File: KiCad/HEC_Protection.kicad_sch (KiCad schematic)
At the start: 19 parts, among them U10 74LS32, U11 74LS00, U11 74LS32, U12 74LS04, U17 74LS74, U18 74LS138, U18 74LS74, U19 74LS30, U22 74LS02, U23 74LS74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

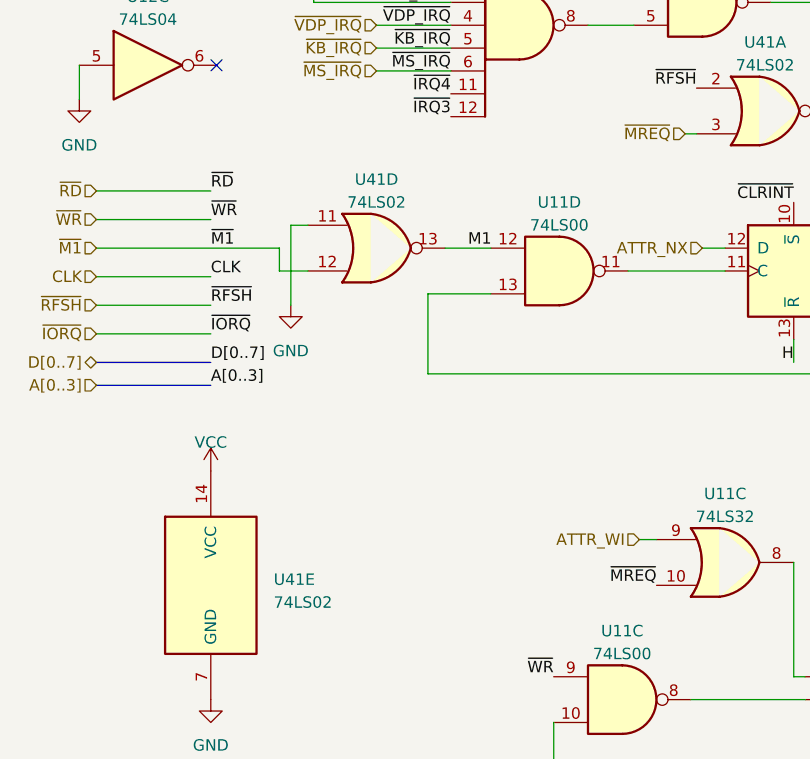
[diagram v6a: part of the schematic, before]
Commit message: Finish routing data bus
finished routing arguably the hardest part of the board: the data bus. The routing is mostly complete. However, the rest of traces are very hard to route. One more day of work is expected.
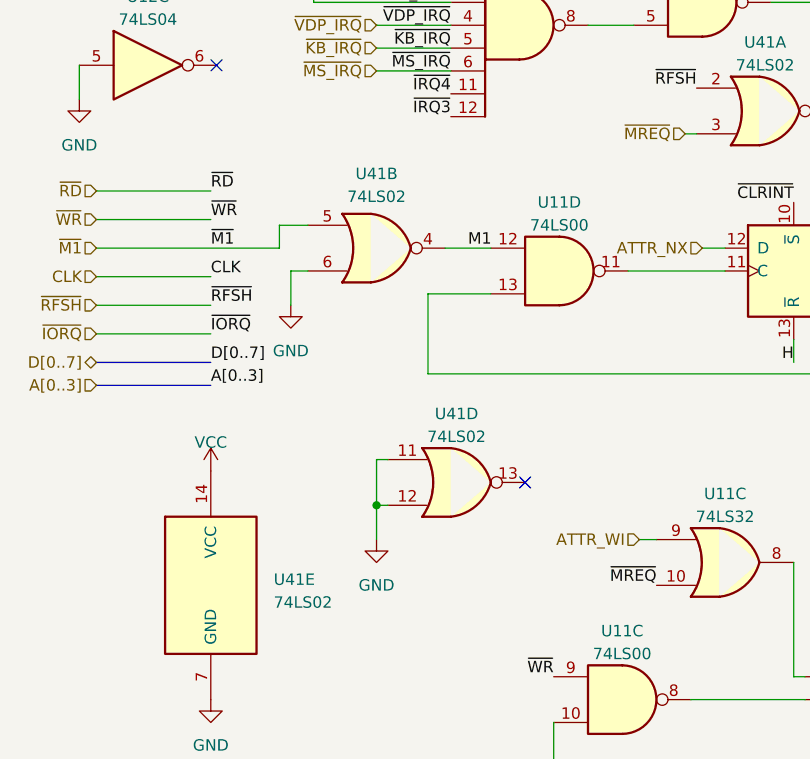
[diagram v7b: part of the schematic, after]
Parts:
- added unit 2 of U41
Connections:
- net GND: now also U41.12, U41.6
- net M1: now also U41.4; no longer U41.13
- net ~{M1}: now also U41.5; no longer U41.12
- no-connect marks 15 -> 16
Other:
- moved on the sheet: U41D
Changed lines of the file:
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@@
   (junction (at 234.315 45.085) (diameter 0) (color 0 0 0 0)
+  )
+  (junction (at 53.34 120.015) (diameter 0) (color 0 0 0 0)
   )
   (junction (at 121.285 139.065) (diameter 0) (color 0 0 0 0)
@@
   (no_connect (at 40.005 36.195))
   (no_connect (at 262.89 90.17))
+  (no_connect (at 69.85 117.475))
   (no_connect (at 165.735 96.52))
   (no_connect (at 116.205 144.145))
@@
     (stroke (width 0) (type default))
   )
+  (wire (pts (xy 53.34 120.015) (xy 54.61 120.015))
+    (stroke (width 0) (type default))
+  )
   (bus (pts (xy 244.475 128.905) (xy 244.475 131.445))
     (stroke (width 0) (type default))
@@
     (stroke (width 0) (type default))
   )
+  (wire (pts (xy 53.34 114.935) (xy 53.34 120.015))
+    (stroke (width 0) (type default))
+  )
   (wire (pts (xy 262.89 29.845) (xy 274.955 29.845))
     (stroke (width 0) (type default))
@@
     (stroke (width 0) (type default))
   )
-  (wire (pts (xy 43.815 88.9) (xy 43.815 97.79))
+  (wire (pts (xy 43.815 93.98) (xy 43.815 97.79))
     (stroke (width 0) (type default))
   )
@@
     (stroke (width 0) (type default))
   )
-  (wire (pts (xy 42.545 93.98) (xy 45.72 93.98))
+  (wire (pts (xy 42.545 88.9) (xy 45.72 88.9))
     (stroke (width 0) (type default))
   )
@@
     (stroke (width 0) (type default))
   )
-  (wire (pts (xy 43.815 88.9) (xy 45.72 88.9))
+  (wire (pts (xy 43.815 93.98) (xy 45.72 93.98))
     (stroke (width 0) (type default))
   )
@@
     (stroke (width 0) (type default))
   )
+  (wire (pts (xy 53.34 120.015) (xy 53.34 123.825))
+    (stroke (width 0) (type default))
+  )
   (wire (pts (xy 189.865 82.55) (xy 192.405 82.55))
     (stroke (width 0) (type default))
@@
     (stroke (width 0) (type default))
   )
+  (wire (pts (xy 54.61 114.935) (xy 53.34 114.935))
+    (stroke (width 0) (type default))
+  )
   (wire (pts (xy 158.75 55.88) (xy 153.67 55.88))
     (stroke (width 0) (type default))
@@
     (stroke (width 0) (type default))
   )
-  (wire (pts (xy 42.545 91.44) (xy 42.545 93.98))
+  (wire (pts (xy 42.545 91.44) (xy 42.545 88.9))
     (stroke (width 0) (type default))
   )
@@
     )
   )
-  (symbol (lib_id "74xx:74LS02") (at 53.34 91.44 0) (unit 4)
-    (in_bom yes) (on_board yes) (dnp no) (fields_autoplaced)
-    (property "Reference" "U41" (at 53.34 83.82 0)
-      (effects (font (size 1.27 1.27)))
-    )
-    (property "Value" "74LS02" (at 53.34 86.36 0)
-      (effects (font (size 1.27 1.27)))
-    )
-    (property "Footprint" "Package_DIP:DIP-14_W7.62mm_Socket" (at 53.34 91.44 0)
-      (effects (font (size 1.27 1.27)) hide)
-    )
-    (property "Datasheet" "http://www.ti.com/lit/gpn/sn74ls02" (at 53.34 91.44 0)
+  (symbol (lib_id "74xx:74LS02") (at 62.23 117.475 0) (unit 4)
+    (in_bom yes) (on_board yes) (dnp no) (fields_autoplaced)
+    (property "Reference" "U41" (at 62.23 109.855 0)
+      (effects (font (size 1.27 1.27)))
+    )
+    (property "Value" "74LS02" (at 62.23 112.395 0)
+      (effects (font (size 1.27 1.27)))
+    )
+    (property "Footprint" "Package_DIP:DIP-14_W7.62mm_Socket" (at 62.23 117.475 0)
+      (effects (font (size 1.27 1.27)) hide)
+    )
+    (property "Datasheet" "http://www.ti.com/lit/gpn/sn74ls02" (at 62.23 117.475 0)
       (effects (font (size 1.27 1.27)) hide)
     )
@@
         (path "/87935374-b60a-4f41-99da-94b76103dd77/2930b625-d6a3-4a7f-9d41-a454efcef99d"
           (reference "U12") (unit 3)
+        )
+      )
+    )
+  )
+  (symbol (lib_id "74xx:74LS32") (at 32.385 36.195 0) (unit 4)
+    (in_bom yes) (on_board yes) (dnp no) (fields_autoplaced)
+    (property "Reference" "U10" (at 32.385 27.94 0)
+      (effects (font (size 1.27 1.27)))
+    )
+    (property "Value" "74LS32" (at 32.385 30.48 0)
+      (effects (font (size 1.27 1.27)))
+    )
+    (property "Footprint" "Package_DIP:DIP-14_W7.62mm_Socket" (at 32.385 36.195 0)
+      (effects (font (size 1.27 1.27)) hide)
+    )
+    (property "Datasheet" "http://www.ti.com/lit/gpn/sn74LS32" (at 32.385 36.195 0)
+      (effects (font (size 1.27 1.27)) hide)
+    )
+    (pin "1")
+    (pin "2")
+    (pin "3")
+    (pin "4")
+    (pin "5")
+    (pin "6")
+    (pin "10")
+    (pin "8")
+    (pin "9")
+    (pin "11")
+    (pin "12")
+    (pin "13")
+    (pin "14")
+    (pin "7")
+    (instances
+      (project "HEC1"
+        (path "/87935374-b60a-4f41-99da-94b76103dd77/933a6f90-eb98-4eb1-8c19-8a76228aece1"
+          (reference "U10") (unit 4)
+        )
+        (path "/87935374-b60a-4f41-99da-94b76103dd77/2930b625-d6a3-4a7f-9d41-a454efcef99d"
+          (reference "U10") (unit 4)
         )
       )
@@
         (path "/87935374-b60a-4f41-99da-94b76103dd77/2930b625-d6a3-4a7f-9d41-a454efcef99d"
           (reference "#PWR037") (unit 1)
-        )
-      )
-    )
-  )
-  (symbol (lib_id "74xx:74LS32") (at 32.385 36.195 0) (unit 4)
-    (in_bom yes) (on_board yes) (dnp no) (fields_autoplaced)
-    (property "Reference" "U10" (at 32.385 27.94 0)
-      (effects (font (size 1.27 1.27)))
-    )
-    (property "Value" "74LS32" (at 32.385 30.48 0)
-      (effects (font (size 1.27 1.27)))
-    )
-    (property "Footprint" "Package_DIP:DIP-14_W7.62mm_Socket" (at 32.385 36.195 0)
-      (effects (font (size 1.27 1.27)) hide)
-    )
-    (property "Datasheet" "http://www.ti.com/lit/gpn/sn74LS32" (at 32.385 36.195 0)
-      (effects (font (size 1.27 1.27)) hide)
-    )
-    (pin "1")
-    (pin "2")
-    (pin "3")
-    (pin "4")
-    (pin "5")
-    (pin "6")
-    (pin "10")
-    (pin "8")
-    (pin "9")
-    (pin "11")
-    (pin "12")
-    (pin "13")
-    (pin "14")
-    (pin "7")
-    (instances
-      (project "HEC1"
-        (path "/87935374-b60a-4f41-99da-94b76103dd77/933a6f90-eb98-4eb1-8c19-8a76228aece1"
-          (reference "U10") (unit 4)
-        )
-        (path "/87935374-b60a-4f41-99da-94b76103dd77/2930b625-d6a3-4a7f-9d41-a454efcef99d"
-          (reference "U10") (unit 4)
         )
       )
@@
     )
   )
+  (symbol (lib_id "74xx:74LS02") (at 53.34 91.44 0) (unit 2)
+    (in_bom yes) (on_board yes) (dnp no) (fields_autoplaced)
+    (property "Reference" "U41" (at 53.34 83.185 0)
+      (effects (font (size 1.27 1.27)))
+    )
+    (property "Value" "74LS02" (at 53.34 85.725 0)
+      (effects (font (size 1.27 1.27)))
+    )
+    (property "Footprint" "Package_DIP:DIP-14_W7.62mm_Socket" (at 53.34 91.44 0)
+      (effects (font (size 1.27 1.27)) hide)
+    )
+    (property "Datasheet" "http://www.ti.com/lit/gpn/sn74ls02" (at 53.34 91.44 0)
+      (effects (font (size 1.27 1.27)) hide)
+    )
+    (pin "1")
+    (pin "2")
+    (pin "3")
+    (pin "4")
+    (pin "5")
+    (pin "6")
+    (pin "10")
+    (pin "8")
+    (pin "9")
+    (pin "11")
+    (pin "12")
+    (pin "13")
+    (pin "14")
+    (pin "7")
+    (instances
+      (project "HEC1"
+        (path "/87935374-b60a-4f41-99da-94b76103dd77/2930b625-d6a3-4a7f-9d41-a454efcef99d"
+          (reference "U41") (unit 2)
+        )
+        (path "/87935374-b60a-4f41-99da-94b76103dd77"
+          (reference "U41") (unit 2)
+        )
+      )
+    )
+  )
   (symbol (lib_id "power:GND") (at 80.01 186.69 0) (unit 1)
     (in_bom yes) (on_board yes) (dnp no) (fields_autoplaced)
@@
         )
       )
+    )
+  )
+  (symbol (lib_id "power:GND") (at 53.34 123.825 0) (unit 1)
+    (in_bom yes) (on_board yes) (dnp no) (fields_autoplaced)
+    (property "Reference" "#PWR0106" (at 53.34 130.175 0)
+      (effects (font (size 1.27 1.27)) hide)
+    )
+    (property "Value" "GND" (at 53.34 128.905 0)
+      (effects (font (size 1.27 1.27)))
+    )
+    (property "Footprint" "" (at 53.34 123.825 0)
+      (effects (font (size 1.27 1.27)) hide)
+    )
+    (property "Datasheet" "" (at 53.34 123.825 0)
+      (effects (font (size 1.27 1.27)) hide)
+    )
+    (pin "1")
+    (instances
+      (project "HEC1"
+        (path "/87935374-b60a-4f41-99da-94b76103dd77"
+          (reference "#PWR0106") (unit 1)
+        )
+        (path "/87935374-b60a-4f41-99da-94b76103dd77/2930b625-d6a3-4a7f-9d41-a454efcef99d"
+          (reference "#PWR0106") (unit 1)
+        )
+      )

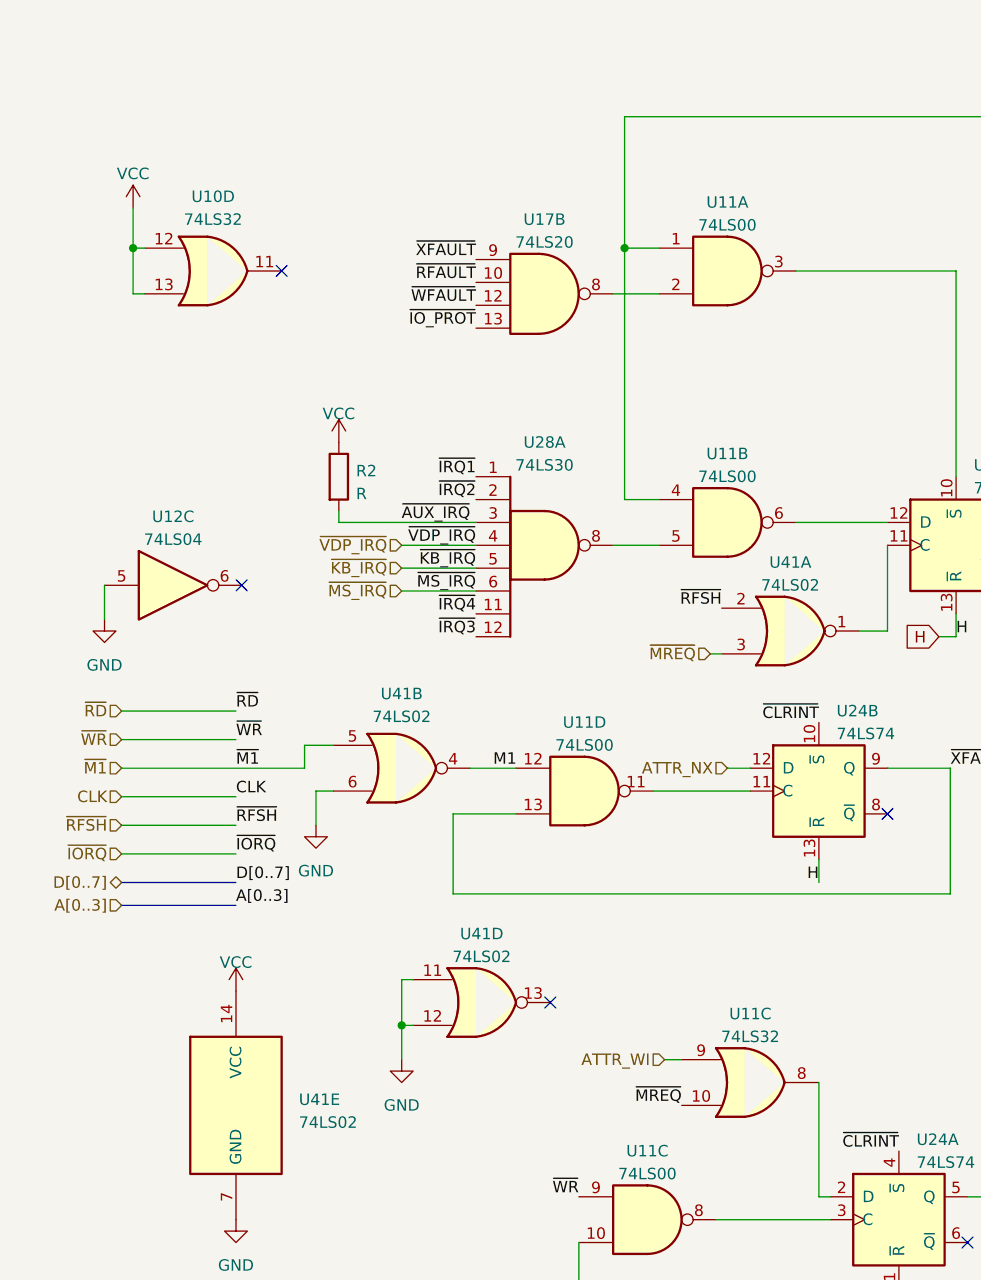
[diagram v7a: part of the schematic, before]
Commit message: Preliminary routing
Changed footprint pad size to allow 2 traces to be routed between adjacent pads. Finished routing all ICs. Bypass caps not added. Some traces may need to be optimized.
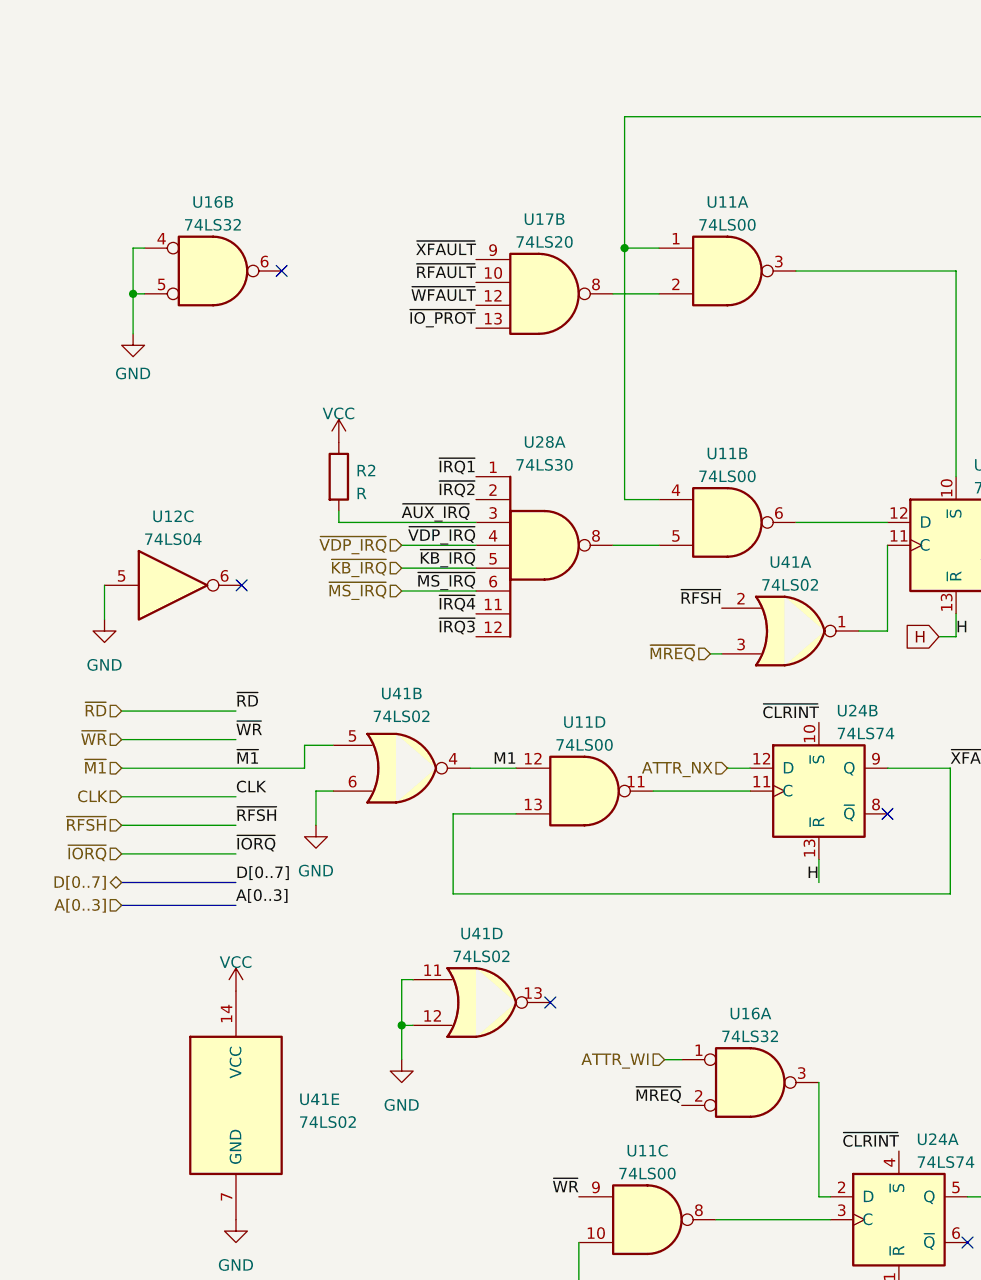
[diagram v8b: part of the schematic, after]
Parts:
- removed U10, U11: 74LS32, Package_DIP:DIP-14_W7.62mm_Socket, symbol 74xx:74LS32
- added U16: 74LS32, Library:DIP-14_W7.62mm_Socket_ThinPads, symbol 74xx:74LS32
- U11, U12, U17, U18, U19, U22, U23, U24, U28, U29, U30, U41: footprint Package_DIP:DIP-14_W7.62mm_Socket -> Library:DIP-14_W7.62mm_Socket_ThinPads
- U18, U8: footprint Package_DIP:DIP-16_W7.62mm_Socket -> Library:DIP-16_W7.62mm_Socket_ThinPads
- U25, U26: footprint Package_DIP:DIP-20_W7.62mm_Socket -> Library:DIP-20_W7.62mm_Socket_ThinPads
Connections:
- net ATTR_WI: now also U16.1
- net GND: now also U16.4, U16.5
- net ~{MREQ}: now also U16.2
- net at U24.2 (D): now also U16.3
